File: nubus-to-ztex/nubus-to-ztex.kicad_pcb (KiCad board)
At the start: 4 copper layers, 161.6 x 100 mm, 99 parts, among them J1 Conn_02x07_Odd_Even, J2 47219-2001, J3 Conn_01x06_Male, J4 C96ABC, J5 HDMI_A, J6 USB micro-B, J7 Conn_01x03_Male, J8 Conn_02x08_Odd_Even, U1 74LVT125, U10 SN65220, U11 TPS2051C, U12 SN74CB3T1G125DBVR, U13 SN74CB3T3125PWR, U14 SN74CB3T3245PWR, U2 74LVT125, U3 74LVT125, U4 SN74CB3T3125PWR, U5 74LVT245BPW,118, U6 74LVT245BPW,118, U7 74LVT245BPW,118, U8 74LVT245BPW,118, U9 TPD12S016PWR

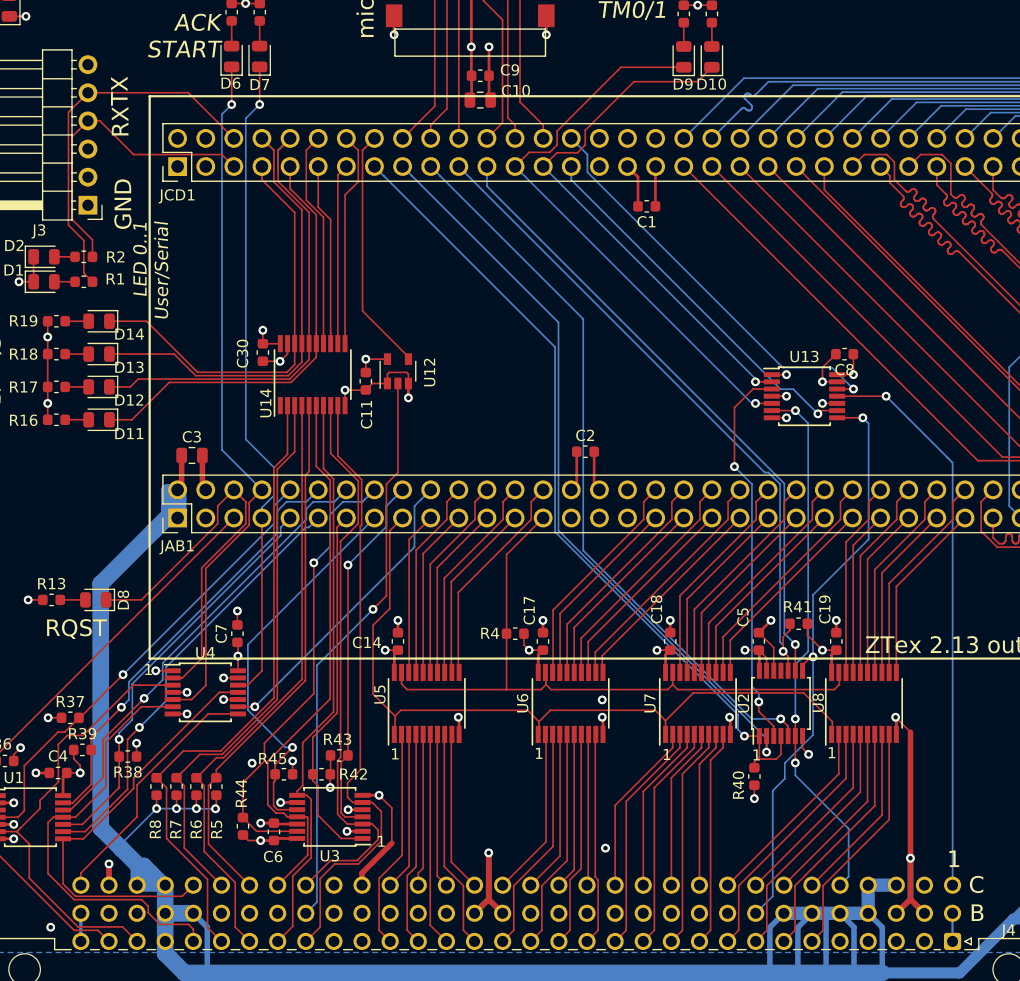
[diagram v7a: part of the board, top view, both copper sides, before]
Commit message: simplify BoM
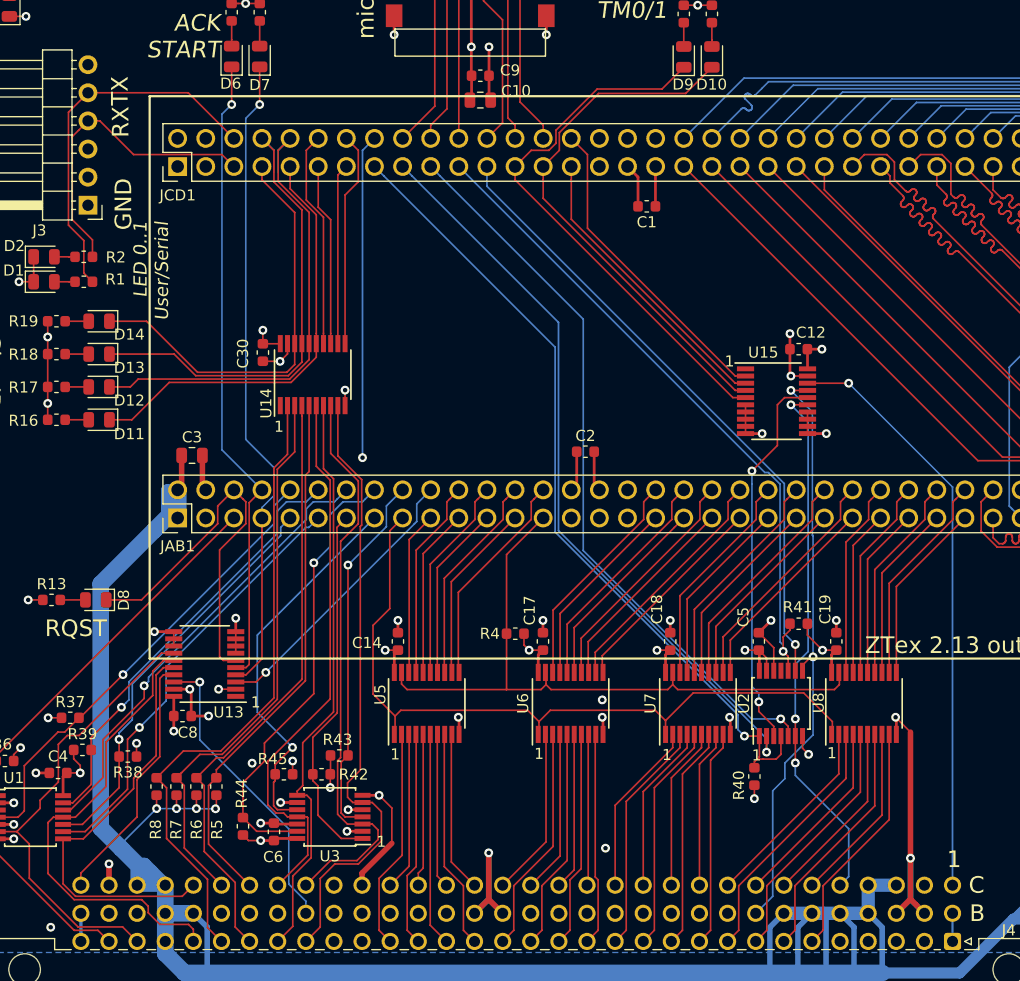
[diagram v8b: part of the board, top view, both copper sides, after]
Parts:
- removed C11, C7: 100nF, Capacitor_SMD:C_0603_1608Metric
- removed U12: SN74CB3T1G125DBVR, Package_TO_SOT_SMD:SOT-23-5
- removed U4: SN74CB3T3125PWR, Package_SO:TSSOP-14_4.4x5mm_P0.65mm
- added C12: 100nF, Capacitor_SMD:C_0603_1608Metric, F.Cu at (186.1, 46.5)
- added U15: SN74CB3T3245PWR, For_SeeedStudio:TSSOP-20_4.4x6.5mm_P0.65mm_ForSeeedStudio, F.Cu at (184.1, 51.2)
- U13: value SN74CB3T3125PWR -> SN74CB3T3245PWR; footprint Package_SO:TSSOP-14_4.4x5mm_P0.65mm -> For_SeeedStudio:TSSOP-20_4.4x6.5mm_P0.65mm_ForSeeedStudio
- moved C8 68.2 mm to (130.4, 79.6), turned to 0 degrees
- moved U13 59.3 mm to (132.4, 74.9), turned to 180 degrees
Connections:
- U13 pad 1: GND -> (no net)
- U13 pad 11: ~RESET_5V -> GND
- U13 pad 12: ~RESET_3V3 -> GND
- U13 pad 14: +3V3 -> ~RQST_5V
- U13 pad 2: ~TM1_3V3 -> ~CLK2X_3V3
- U13 pad 3: ~TM1_5V -> ~CLK_3V3
- U13 pad 4: GND -> ~START_3V3
- U13 pad 5: ~TM0_3V3 -> ~ACK_3V3
- U13 pad 6: ~TM0_5V -> ~RQST_3V3
- U13 pad 8: ~TM2_5V -> GND
- U13 pad 9: ~TM2_3V3 -> GND
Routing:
- net +3V3: track 720.3 -> 670.1 mm, vias 29 -> 28
- net ~CLK2X_3V3: track 22.4 -> 57.1 mm, vias 0 -> 2
- net ~CLK2X_5V: track 51.3 -> 27.2 mm
- net ~RESET_3V3: track 37.3 -> 28.5 mm, vias 1 -> 0
- net ~TM2_3V3: track 34.1 -> 26.6 mm, vias 1 -> 0
- net ~ACK_3V3: track 63.4 -> 57.7 mm
- net ~ACK_5V: track 39.2 -> 42.3 mm
- net ~RQST_3V3: track 37.3 -> 34.7 mm
- net ~CLK_3V3: track 27.7 -> 25.7 mm
- net ~TM0_3V3: track 51.7 -> 49.8 mm, vias 1 -> 0
- net ~RESET_5V: track 51.1 -> 53.0 mm
- net ~RQST_5V: track 40.5 -> 41.8 mm
- net ARB3_o_n: track 35.8 -> 34.7 mm
- net ~START_3V3: track 59.3 -> 58.5 mm
- net ~START_5V: track 38.5 -> 37.9 mm
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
